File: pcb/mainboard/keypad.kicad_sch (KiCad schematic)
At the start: 8 parts

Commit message: Working on mainboard schematics
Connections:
- net +3V3 is gone; now on net +1V8: R?.1, R?.1
- net LCD_RST: now reaches U?.AF11 (GPIO1_IO07)
- net AVDD_EN: now reaches U?.AF12 (GPIO1_IO05)
- net PMIC_INT: now reaches U?.AF13 (GPIO1_IO03)
- net VNEG_CTRL: now reaches U?.AG11 (GPIO1_IO06)
- net SD2_VSEL: now reaches U?.AG12 (GPIO1_IO04)
- net WDOG_B: now reaches U?.AG13 (GPIO1_IO02)
- net REF_CLK_32K: now reaches U?.AG14 (GPIO1_IO00)
- net UART1_RTS: now reaches U?.D18 (UART3_TXD)
- net UART1_RXD: now reaches U?.E14 (UART1_RXD)
- net UART1_CTS: now reaches U?.E18 (UART3_RXD)
- net UART1_TXD: now reaches U?.F13 (UART1_TXD)
- net UART4_TXD: now reaches U?.F18 (UART4_TXD)
- net UART4_RXD: now reaches U?.F19 (UART4_RXD)
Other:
- moved on the sheet: R?, U?F

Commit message: Mainboard schematics WIP
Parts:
- gave numbers to parts that had none: 5
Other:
- moved on the sheet: U201K
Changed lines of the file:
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@@
     (stroke (width 0) (type default) (color 0 0 0 0))
   )
-  (wire (pts (xy 147.32 50.8) (xy 149.86 50.8))
+  (wire (pts (xy 139.7 50.8) (xy 142.24 50.8))
     (stroke (width 0) (type default) (color 0 0 0 0))
   )
-  (wire (pts (xy 147.32 60.96) (xy 149.86 60.96))
+  (wire (pts (xy 139.7 60.96) (xy 142.24 60.96))
     (stroke (width 0) (type default) (color 0 0 0 0))
   )
@@
     (stroke (width 0) (type default) (color 0 0 0 0))
   )
-  (wire (pts (xy 147.32 53.34) (xy 149.86 53.34))
+  (wire (pts (xy 139.7 53.34) (xy 142.24 53.34))
     (stroke (width 0) (type default) (color 0 0 0 0))
   )
@@
     (stroke (width 0) (type solid) (color 0 0 0 0))
   )
-  (wire (pts (xy 147.32 45.72) (xy 149.86 45.72))
+  (wire (pts (xy 139.7 45.72) (xy 142.24 45.72))
     (stroke (width 0) (type default) (color 0 0 0 0))
   )
@@
     (stroke (width 0) (type solid) (color 0 0 0 0))
   )
-  (wire (pts (xy 147.32 58.42) (xy 149.86 58.42))
+  (wire (pts (xy 139.7 58.42) (xy 142.24 58.42))
     (stroke (width 0) (type default) (color 0 0 0 0))
   )
@@
     (stroke (width 0) (type solid) (color 0 0 0 0))
   )
-  (wire (pts (xy 147.32 63.5) (xy 149.86 63.5))
+  (wire (pts (xy 139.7 63.5) (xy 142.24 63.5))
     (stroke (width 0) (type default) (color 0 0 0 0))
   )
@@
     (stroke (width 0) (type solid) (color 0 0 0 0))
   )
-  (wire (pts (xy 147.32 55.88) (xy 149.86 55.88))
+  (wire (pts (xy 139.7 55.88) (xy 142.24 55.88))
     (stroke (width 0) (type default) (color 0 0 0 0))
   )
@@
     (stroke (width 0) (type solid) (color 0 0 0 0))
   )
-  (global_label "WDOG_B" (shape output) (at 149.86 50.8 0) (fields_autoplaced)
+  (global_label "WDOG_B" (shape output) (at 142.24 50.8 0) (fields_autoplaced)
     (effects (font (size 1.27 1.27)) (justify left))
-    (property "Intersheet References" "${INTERSHEET_REFS}" (id 0) (at 160.0231 50.8794 0)
+    (property "Intersheet References" "${INTERSHEET_REFS}" (id 0) (at 152.4031 50.8794 0)
       (effects (font (size 1.27 1.27)) (justify left) hide)
     )
@@
     )
   )
-  (global_label "REF_CLK_32K" (shape output) (at 149.86 45.72 0) (fields_autoplaced)
+  (global_label "REF_CLK_32K" (shape output) (at 142.24 45.72 0) (fields_autoplaced)
     (effects (font (size 1.27 1.27)) (justify left))
-    (property "Intersheet References" "${INTERSHEET_REFS}" (id 0) (at 165.1636 45.6406 0)
+    (property "Intersheet References" "${INTERSHEET_REFS}" (id 0) (at 157.5436 45.6406 0)
       (effects (font (size 1.27 1.27)) (justify left) hide)
     )
@@
     )
   )
-  (global_label "AVDD_EN" (shape output) (at 149.86 58.42 0) (fields_autoplaced)
+  (global_label "AVDD_EN" (shape output) (at 142.24 58.42 0) (fields_autoplaced)
     (effects (font (size 1.27 1.27)) (justify left))
-    (property "Intersheet References" "${INTERSHEET_REFS}" (id 0) (at 160.6279 58.3406 0)
+    (property "Intersheet References" "${INTERSHEET_REFS}" (id 0) (at 153.0079 58.3406 0)
       (effects (font (size 1.27 1.27)) (justify left) hide)
     )
@@
     )
   )
-  (global_label "PMIC_INT" (shape input) (at 149.86 53.34 0) (fields_autoplaced)
+  (global_label "PMIC_INT" (shape input) (at 142.24 53.34 0) (fields_autoplaced)
     (effects (font (size 1.27 1.27)) (justify left))
-    (property "Intersheet References" "${INTERSHEET_REFS}" (id 0) (at 160.9303 53.2606 0)
+    (property "Intersheet References" "${INTERSHEET_REFS}" (id 0) (at 153.3103 53.2606 0)
       (effects (font (size 1.27 1.27)) (justify left) hide)
     )
@@
     )
   )
-  (global_label "VNEG_CTRL" (shape output) (at 149.86 60.96 0) (fields_autoplaced)
+  (global_label "VNEG_CTRL" (shape output) (at 142.24 60.96 0) (fields_autoplaced)
     (effects (font (size 1.27 1.27)) (justify left))
-    (property "Intersheet References" "${INTERSHEET_REFS}" (id 0) (at 162.805 60.8806 0)
+    (property "Intersheet References" "${INTERSHEET_REFS}" (id 0) (at 155.185 60.8806 0)
       (effects (font (size 1.27 1.27)) (justify left) hide)
     )
   )
-  (global_label "LCD_RST" (shape output) (at 149.86 63.5 0)
+  (global_label "LCD_RST" (shape output) (at 142.24 63.5 0)
     (effects (font (size 1.27 1.27)) (justify left))
-    (property "Intersheet References" "${INTERSHEET_REFS}" (id 0) (at 161.78 63.4206 0)
+    (property "Intersheet References" "${INTERSHEET_REFS}" (id 0) (at 154.16 63.4206 0)
       (effects (font (size 1.27 1.27)) (justify left) hide)
     )
@@
     )
   )
-  (global_label "SD2_VSEL" (shape output) (at 149.86 55.88 0) (fields_autoplaced)
+  (global_label "SD2_VSEL" (shape output) (at 142.24 55.88 0) (fields_autoplaced)
     (effects (font (size 1.27 1.27)) (justify left))
-    (property "Intersheet References" "${INTERSHEET_REFS}" (id 0) (at 161.5955 55.8006 0)
+    (property "Intersheet References" "${INTERSHEET_REFS}" (id 0) (at 153.9755 55.8006 0)
       (effects (font (size 1.27 1.27)) (justify left) hide)
     )
@@
   (symbol (lib_id "Device:R") (at 162.56 107.95 0) (unit 1)
     (in_bom yes) (on_board yes)
-    (property "Reference" "R?" (id 0) (at 165.1 106.68 0)
+    (property "Reference" "R603" (id 0) (at 165.1 106.68 0)
       (effects (font (size 1.27 1.27)) (justify left))
     )
@@
   (symbol (lib_id "symbols:MIMX8MN6DVTJZAA") (at 233.68 43.18 0) (unit 10)
     (in_bom yes) (on_board yes) (fields_autoplaced)
-    (property "Reference" "U?" (id 0) (at 233.68 43.18 0))
+    (property "Reference" "U201" (id 0) (at 233.68 43.18 0))
     (property "Value" "MIMX8MN6DVTJZAA" (id 1) (at 233.68 45.72 0))
     (property "Footprint" "footprint:BGA-486_27x27_14.0x14.0mm" (id 2) (at 233.68 43.18 0)
@@
   (symbol (lib_id "Device:R") (at 172.72 107.95 0) (unit 1)
     (in_bom yes) (on_board yes)
-    (property "Reference" "R?" (id 0) (at 175.26 106.68 0)
+    (property "Reference" "R604" (id 0) (at 175.26 106.68 0)
       (effects (font (size 1.27 1.27)) (justify left))
     )
@@
   (symbol (lib_id "Device:R") (at 152.4 107.95 0) (unit 1)
     (in_bom yes) (on_board yes)
-    (property "Reference" "R?" (id 0) (at 154.94 106.68 0)
+    (property "Reference" "R602" (id 0) (at 154.94 106.68 0)
       (effects (font (size 1.27 1.27)) (justify left))
     )
@@
     (pin "2")
   )
-  (symbol (lib_id "symbols:MIMX8MN6DVTJZAA") (at 127 35.56 0) (unit 11)
+  (symbol (lib_id "symbols:MIMX8MN6DVTJZAA") (at 119.38 35.56 0) (unit 11)
     (in_bom yes) (on_board yes) (fields_autoplaced)
-    (property "Reference" "U?" (id 0) (at 127 35.56 0))
-    (property "Value" "MIMX8MN6DVTJZAA" (id 1) (at 127 38.1 0))
-    (property "Footprint" "footprint:BGA-486_27x27_14.0x14.0mm" (id 2) (at 127 35.56 0)
+    (property "Reference" "U201" (id 0) (at 119.38 35.56 0))
+    (property "Value" "MIMX8MN6DVTJZAA" (id 1) (at 119.38 38.1 0))
+    (property "Footprint" "footprint:BGA-486_27x27_14.0x14.0mm" (id 2) (at 119.38 35.56 0)
       (effects (font (size 1.27 1.27)) hide)
     )
-    (property "Datasheet" "" (id 3) (at 127 35.56 0)
+    (property "Datasheet" "" (id 3) (at 119.38 35.56 0)
       (effects (font (size 1.27 1.27)) hide)
     )
@@
   (symbol (lib_id "symbols:MIMX8MN6DVTJZAA") (at 119.38 109.22 0) (unit 6)
     (in_bom yes) (on_board yes) (fields_autoplaced)
-    (property "Reference" "U?" (id 0) (at 119.38 109.22 0))
+    (property "Reference" "U201" (id 0) (at 119.38 109.22 0))
     (property "Value" "MIMX8MN6DVTJZAA" (id 1) (at 119.38 111.76 0))
     (property "Footprint" "footprint:BGA-486_27x27_14.0x14.0mm" (id 2) (at 119.38 109.22 0)
@@
   (symbol (lib_id "symbols:MIMX8MN6DVTJZAA") (at 233.68 99.06 0) (unit 3)
     (in_bom yes) (on_board yes) (fields_autoplaced)
-    (property "Reference" "U?" (id 0) (at 233.68 99.06 0))
+    (property "Reference" "U201" (id 0) (at 233.68 99.06 0))
     (property "Value" "MIMX8MN6DVTJZAA" (id 1) (at 233.68 101.6 0))
     (property "Footprint" "footprint:BGA-486_27x27_14.0x14.0mm" (id 2) (at 233.68 99.06 0)
@@
   (symbol (lib_id "power:+1V8") (at 142.24 104.14 0) (unit 1)
     (in_bom yes) (on_board yes)
-    (property "Reference" "#PWR?" (id 0) (at 142.24 107.95 0)
+    (property "Reference" "#PWR0601" (id 0) (at 142.24 107.95 0)
       (effects (font (size 1.27 1.27)) hide)
     )
@@
   (symbol (lib_id "Device:R") (at 142.24 107.95 0) (unit 1)
     (in_bom yes) (on_board yes)
-    (property "Reference" "R?" (id 0) (at 144.78 106.68 0)
+    (property "Reference" "R601" (id 0) (at 144.78 106.68 0)
       (effects (font (size 1.27 1.27)) (justify left))
     )

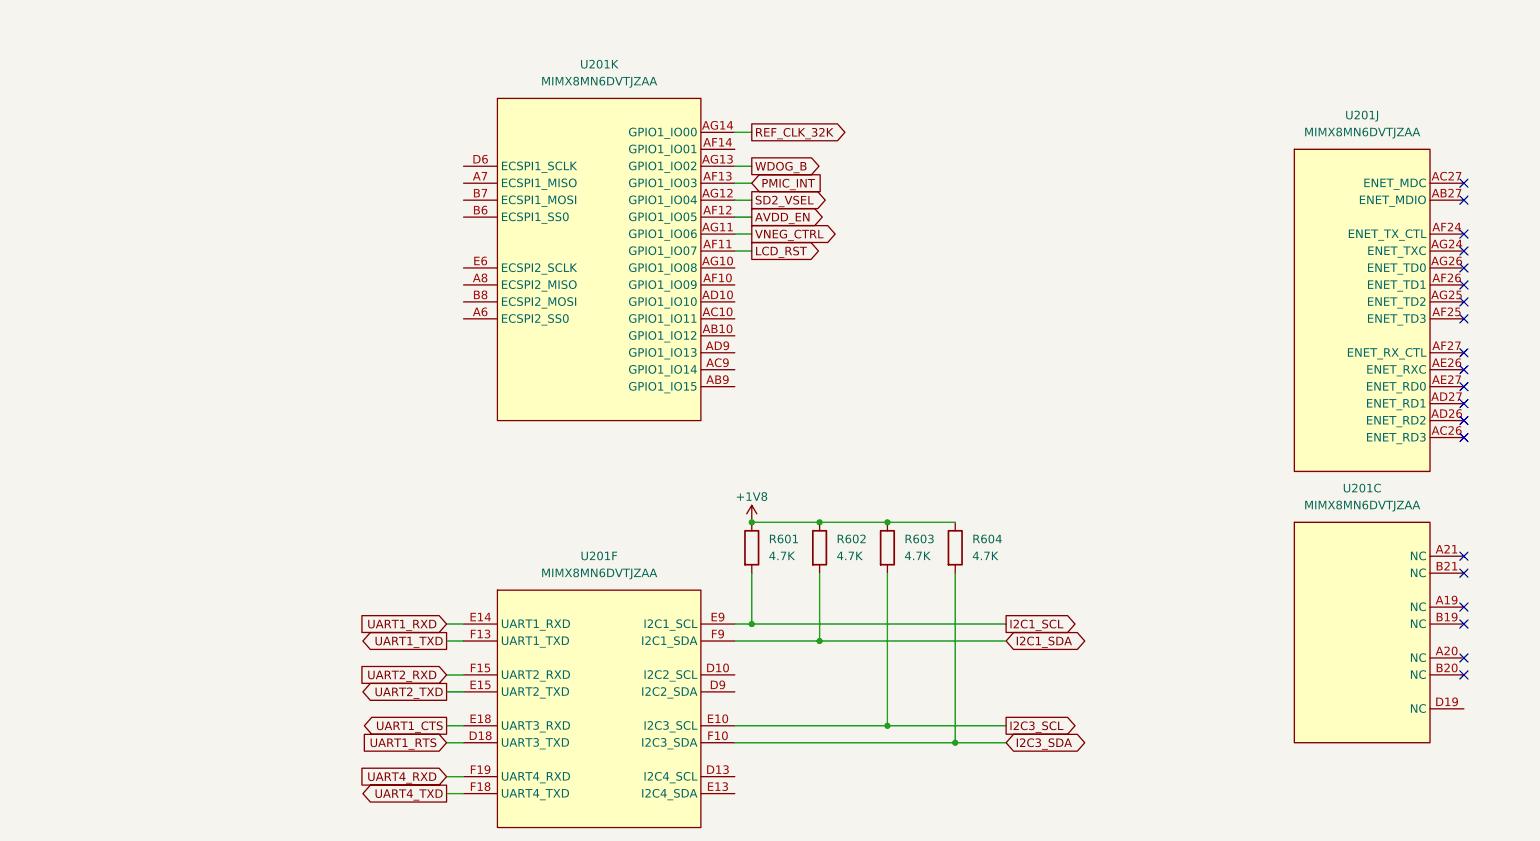
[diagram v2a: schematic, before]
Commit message: Draft motherboard schematics for r0.0 layout
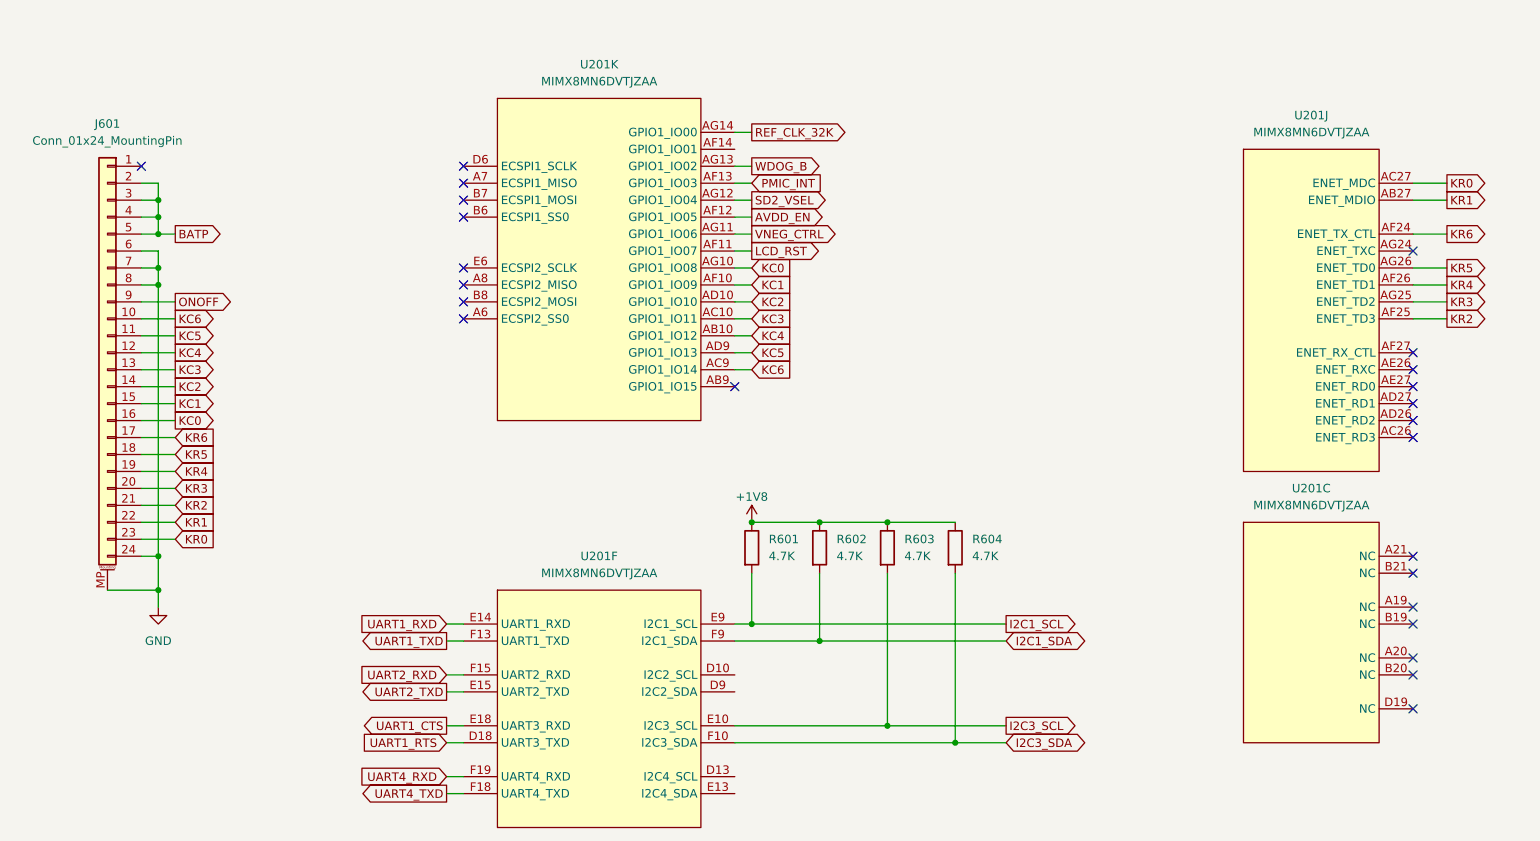
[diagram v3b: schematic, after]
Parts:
- added J601: Conn_01x24_MountingPin, Connector_FFC-FPC:TE_2-1734839-4_1x24-1MP_P0.5mm_Horizontal, symbol Connector_Generic_MountingPin:Conn_01x24_MountingPin
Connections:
- net KR1: now reaches U201.AB27 (ENET_MDIO)
- net KR1: now also J601.22 (Pin_22)
- net KR0: now reaches U201.AC27 (ENET_MDC)
- net KR0: now also J601.23 (Pin_23)
- net KR6: now reaches U201.AF24 (ENET_TX_CTL)
- net KR6: now also J601.17 (Pin_17)
- net KR2: now reaches U201.AF25 (ENET_TD3)
- net KR2: now also J601.21 (Pin_21)
- net KR4: now reaches U201.AF26 (ENET_TD1)
- net KR4: now also J601.19 (Pin_19)
- net KR3: now reaches U201.AG25 (ENET_TD2)
- net KR3: now also J601.20 (Pin_20)
- net KR5: now reaches U201.AG26 (ENET_TD0)
- net KR5: now also J601.18 (Pin_18)
- net KC4: now reaches U201.AB10 (GPIO1_IO12)
- net KC4: now also J601.12 (Pin_12)
- net KC3: now reaches U201.AC10 (GPIO1_IO11)
- net KC3: now also J601.13 (Pin_13)
- net KC6: now reaches U201.AC9 (GPIO1_IO14)
- net KC6: now also J601.10 (Pin_10)
- net KC2: now reaches U201.AD10 (GPIO1_IO10)
- net KC2: now also J601.14 (Pin_14)
- net KC5: now reaches U201.AD9 (GPIO1_IO13)
- net KC5: now also J601.11 (Pin_11)
- net KC1: now reaches U201.AF10 (GPIO1_IO09)
- net KC1: now also J601.15 (Pin_15)
- net KC0: now reaches U201.AG10 (GPIO1_IO08)
- net KC0: now also J601.16 (Pin_16)
- new net BATP: J601.2 (Pin_2), J601.3 (Pin_3), J601.4 (Pin_4), J601.5 (Pin_5)
- new net GND: J601.24 (Pin_24), J601.6 (Pin_6), J601.7 (Pin_7), J601.8 (Pin_8), J601.MP (MountPin)
- new net ONOFF: J601.9 (Pin_9)
- no-connect marks 20 -> 24
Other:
- moved on the sheet: U201C, U201J

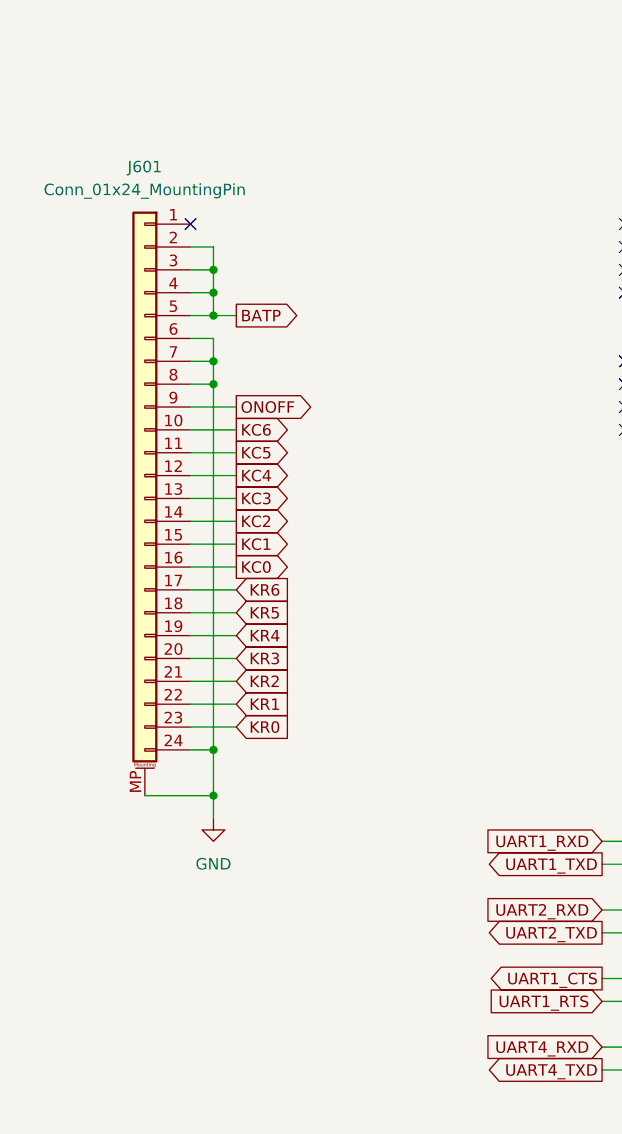
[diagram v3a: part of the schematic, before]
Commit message: Motherboard PCB component initial placement, schematics fixes
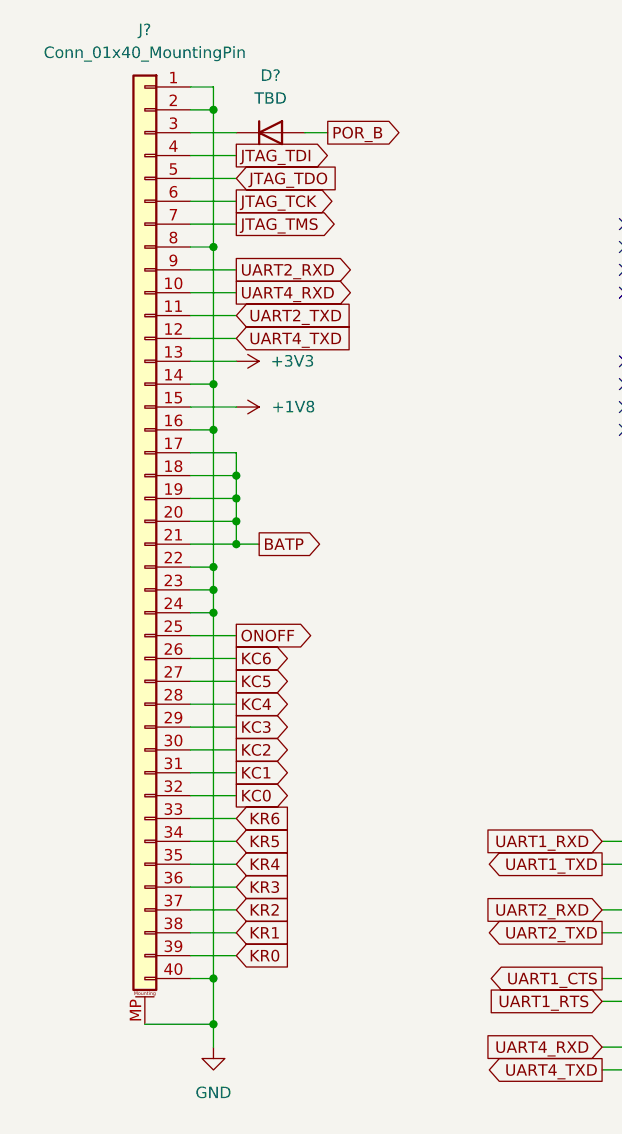
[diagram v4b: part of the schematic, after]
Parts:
- removed J601: Conn_01x24_MountingPin, Connector_FFC-FPC:TE_2-1734839-4_1x24-1MP_P0.5mm_Horizontal, symbol Connector_Generic_MountingPin:Conn_01x24_MountingPin
- added D?: TBD, Diode_SMD:D_SOD-323, symbol Device:D
- added J?: Conn_01x40_MountingPin, Connector_FFC-FPC:TE_4-1734839-0_1x40-1MP_P0.5mm_Horizontal, symbol Connector_Generic_MountingPin:Conn_01x40_MountingPin
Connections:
- net +1V8: now also J?.15 (Pin_15)
- net BATP: now also J?.17 (Pin_17), J?.18 (Pin_18), J?.19 (Pin_19), J?.20 (Pin_20), J?.21 (Pin_21)
- net GND: now also J?.1 (Pin_1), J?.14 (Pin_14), J?.16 (Pin_16), J?.2 (Pin_2), J?.22 (Pin_22), J?.23 (Pin_23), J?.24 (Pin_24), J?.40 (Pin_40), J?.8 (Pin_8), J?.MP (MountPin)
- net KC0: now also J?.32 (Pin_32)
- net KC1: now also J?.31 (Pin_31)
- net KC2: now also J?.30 (Pin_30)
- net KC3: now also J?.29 (Pin_29)
- net KC4: now also J?.28 (Pin_28)
- net KC5: now also J?.27 (Pin_27)
- net KC6: now also J?.26 (Pin_26)
- net KR0: now also J?.39 (Pin_39)
- net KR1: now also J?.38 (Pin_38)
- net KR2: now also J?.37 (Pin_37)
- net KR3: now also J?.36 (Pin_36)
- net KR4: now also J?.35 (Pin_35)
- net KR5: now also J?.34 (Pin_34)
- net KR6: now also J?.33 (Pin_33)
- net ONOFF: now also J?.25 (Pin_25)
- net UART2_RXD: now also J?.9 (Pin_9)
- net UART2_TXD: now also J?.11 (Pin_11)
- net UART4_RXD: now also J?.10 (Pin_10)
- net UART4_TXD: now also J?.12 (Pin_12)
- new net: D?.1 (K), J?.3 (Pin_3)
- new net +3V3: J?.13 (Pin_13)
- new net JTAG_TCK: J?.6 (Pin_6)
- new net JTAG_TDI: J?.4 (Pin_4)
- new net JTAG_TDO: J?.5 (Pin_5)
- new net JTAG_TMS: J?.7 (Pin_7)
- new net POR_B: D?.2 (A)
- no-connect marks 24 -> 23
